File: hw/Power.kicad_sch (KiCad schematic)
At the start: 1 part

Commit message: setup components information
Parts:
- BT?: footprint (none) -> Battery:BatteryHolder_Keystone_2460_1xAA
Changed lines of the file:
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@@
       (effects (font (size 1.27 1.27)) (justify left))
     )
-    (property "Footprint" "" (at 142.24 35.306 90)
+    (property "Footprint" "Battery:BatteryHolder_Keystone_2460_1xAA" (at 142.24 35.306 90)
       (effects (font (size 1.27 1.27)) hide)
     )

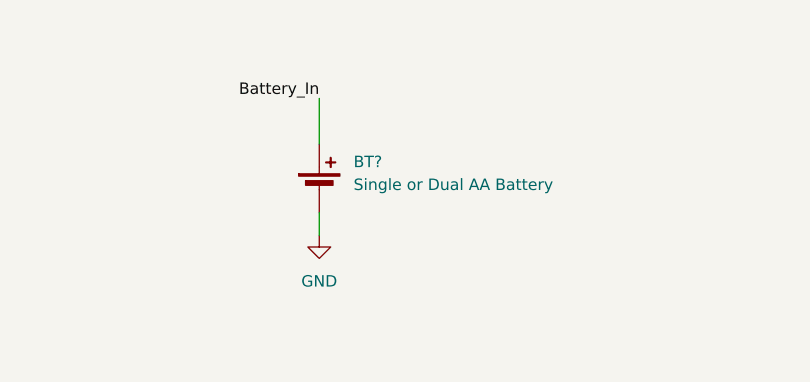
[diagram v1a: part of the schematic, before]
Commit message: added switches
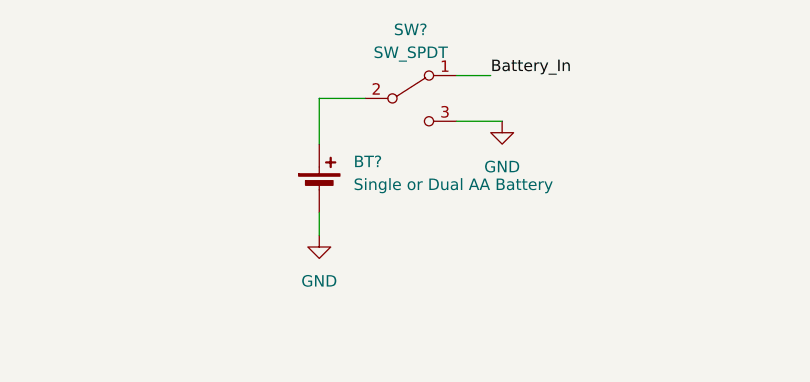
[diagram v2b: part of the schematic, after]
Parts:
- added SW?: SW_SPDT, IotPi_Switch:MS-22D28-G020, symbol Switch:SW_SPDT
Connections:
- net Battery_In: now also SW?.1 (A); no longer BT?.1 (+)
- net GND: now also SW?.3 (C)
- new net: BT?.1 (+), SW?.2 (B)
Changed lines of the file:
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@@
+    (stroke (width 0) (type default))
+  )
+  (wire (pts (xy 157.48 24.13) (xy 161.29 24.13))
+    (stroke (width 0) (type default))
+  )
+  (wire (pts (xy 142.24 26.67) (xy 147.32 26.67))
     (stroke (width 0) (type default))
   )
@@
   )
   (wire (pts (xy 142.24 39.37) (xy 142.24 41.91))
+    (stroke (width 0) (type default))
+  )
+  (wire (pts (xy 157.48 29.21) (xy 162.56 29.21))
     (stroke (width 0) (type default))
   )
@@
     (effects (font (size 1.27 1.27)) (justify right bottom))
   )
-  (label "Battery_In" (at 142.24 26.67 180) (fields_autoplaced)
-    (effects (font (size 1.27 1.27)) (justify right bottom))
+  (label "Battery_In" (at 161.29 24.13 0) (fields_autoplaced)
+    (effects (font (size 1.27 1.27)) (justify left bottom))
   )
   (label "VOUT_3V3" (at 78.74 76.2 180) (fields_autoplaced)
@@
   (hierarchical_label "VBUS" (shape input) (at 43.18 30.48 180) (fields_autoplaced)
     (effects (font (size 1.27 1.27)) (justify right))
+  )
+  (symbol (lib_id "power:GND") (at 162.56 29.21 0) (unit 1)
+    (in_bom yes) (on_board yes) (dnp no) (fields_autoplaced)
+    (property "Reference" "#PWR?" (at 162.56 35.56 0)
+      (effects (font (size 1.27 1.27)) hide)
+    )
+    (property "Value" "GND" (at 162.56 34.29 0)
+      (effects (font (size 1.27 1.27)))
+    )
+    (property "Footprint" "" (at 162.56 29.21 0)
+      (effects (font (size 1.27 1.27)) hide)
+    )
+    (property "Datasheet" "" (at 162.56 29.21 0)
+      (effects (font (size 1.27 1.27)) hide)
+    )
+    (pin "1")
+    (instances
+      (project "KiConSZ2023"
+        (path "/8659c260-f029-4e72-8b9a-85fff45eea40/f453823a-a381-482a-9343-94fafcdcaf18"
+          (reference "#PWR?") (unit 1)
+        )
+      )
+    )
   )
   (symbol (lib_id "Device:Battery_Cell") (at 142.24 36.83 0) (unit 1)
@@
   (symbol (lib_id "power:GND") (at 142.24 41.91 0) (unit 1)
     (in_bom yes) (on_board yes) (dnp no) (fields_autoplaced)
-    (property "Reference" "#PWR05901" (at 142.24 48.26 0)
+    (property "Reference" "#PWR?" (at 142.24 48.26 0)
       (effects (font (size 1.27 1.27)) hide)
     )
@@
       (project "KiConSZ2023"
         (path "/8659c260-f029-4e72-8b9a-85fff45eea40/f453823a-a381-482a-9343-94fafcdcaf18"
-          (reference "#PWR05901") (unit 1)
+          (reference "#PWR?") (unit 1)
         )
       )
+    )
+  )
+  (symbol (lib_id "Switch:SW_SPDT") (at 152.4 26.67 0) (unit 1)
+    (in_bom yes) (on_board yes) (dnp no) (fields_autoplaced)
+    (property "Reference" "SW?" (at 152.4 19.05 0)
+      (effects (font (size 1.27 1.27)))
+    )
+    (property "Value" "SW_SPDT" (at 152.4 21.59 0)
+      (effects (font (size 1.27 1.27)))
+    )
+    (property "Footprint" "IotPi_Switch:MS-22D28-G020" (at 152.4 26.67 0)
+      (effects (font (size 1.27 1.27)) hide)
+    )
+    (property "Datasheet" "~" (at 152.4 26.67 0)
+      (effects (font (size 1.27 1.27)) hide)
+    )
+    (pin "1")
+    (pin "2")
+    (pin "3")
+    (instances
+      (project "KiConSZ2023"
+        (path "/8659c260-f029-4e72-8b9a-85fff45eea40/f453823a-a381-482a-9343-94fafcdcaf18"
+          (reference "SW?") (unit 1)
+        )
+      )

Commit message: annotations
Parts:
- gave numbers to parts that had none: 2
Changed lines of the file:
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@@
   (symbol (lib_id "power:GND") (at 162.56 29.21 0) (unit 1)
     (in_bom yes) (on_board yes) (dnp no) (fields_autoplaced)
-    (property "Reference" "#PWR?" (at 162.56 35.56 0)
+    (property "Reference" "#PWR010" (at 162.56 35.56 0)
       (effects (font (size 1.27 1.27)) hide)
     )
@@
       (project "KiConSZ2023"
         (path "/8659c260-f029-4e72-8b9a-85fff45eea40/f453823a-a381-482a-9343-94fafcdcaf18"
-          (reference "#PWR?") (unit 1)
+          (reference "#PWR010") (unit 1)
         )
       )
@@
   (symbol (lib_id "Device:Battery_Cell") (at 142.24 36.83 0) (unit 1)
     (in_bom yes) (on_board yes) (dnp no) (fields_autoplaced)
-    (property "Reference" "BT?" (at 146.05 33.7185 0)
+    (property "Reference" "BT2" (at 146.05 33.7185 0)
       (effects (font (size 1.27 1.27)) (justify left))
     )
@@
       (project "KiConSZ2023"
         (path "/8659c260-f029-4e72-8b9a-85fff45eea40/f453823a-a381-482a-9343-94fafcdcaf18"
-          (reference "BT?") (unit 1)
+          (reference "BT2") (unit 1)
         )
       )
@@
   (symbol (lib_id "power:GND") (at 142.24 41.91 0) (unit 1)
     (in_bom yes) (on_board yes) (dnp no) (fields_autoplaced)
-    (property "Reference" "#PWR?" (at 142.24 48.26 0)
+    (property "Reference" "#PWR09" (at 142.24 48.26 0)
       (effects (font (size 1.27 1.27)) hide)
     )
@@
       (project "KiConSZ2023"
         (path "/8659c260-f029-4e72-8b9a-85fff45eea40/f453823a-a381-482a-9343-94fafcdcaf18"
-          (reference "#PWR?") (unit 1)
+          (reference "#PWR09") (unit 1)
         )
       )
@@
   (symbol (lib_id "Switch:SW_SPDT") (at 152.4 26.67 0) (unit 1)
     (in_bom yes) (on_board yes) (dnp no) (fields_autoplaced)
-    (property "Reference" "SW?" (at 152.4 19.05 0)
+    (property "Reference" "SW4" (at 152.4 19.05 0)
       (effects (font (size 1.27 1.27)))
     )
@@
       (project "KiConSZ2023"
         (path "/8659c260-f029-4e72-8b9a-85fff45eea40/f453823a-a381-482a-9343-94fafcdcaf18"
-          (reference "SW?") (unit 1)
+          (reference "SW4") (unit 1)
         )
       )

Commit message: updated LCSC of switches
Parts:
- SW4: LCSC (none) -> C963205; Vendor (none) -> G-Switch(品赞); Vendor Model (none) -> MS-22D28-G020
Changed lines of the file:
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@@
+      (effects (font (size 1.27 1.27)) hide)
+    )
+    (property "Description" "额定电流(DC): 1A 额定电压(DC): 6V 电路结构: 双刀双掷 安装方式: 立贴 机械寿命: 10000次 开关颜色: 黑色 滑钮" (at 152.4 26.67 0)
+      (effects (font (size 1.27 1.27)) hide)
+    )
+    (property "LCSC" "C963205" (at 152.4 26.67 0)
+      (effects (font (size 1.27 1.27)) hide)
+    )
+    (property "Vendor" "G-Switch(品赞)" (at 152.4 26.67 0)
+      (effects (font (size 1.27 1.27)) hide)
+    )
+    (property "Vendor Model" "MS-22D28-G020" (at 152.4 26.67 0)
       (effects (font (size 1.27 1.27)) hide)
     )

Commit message: updated netclasses
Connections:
- net Battery_Holder_In: now reaches BT2.1 (+), SW4.2 (B)
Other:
- moved on the sheet: BT2, SW4
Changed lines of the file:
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@@
 (kicad_sch (version 20230121) (generator eeschema)
   (paper "A4")
-  (wire (pts (xy 142.24 31.75) (xy 142.24 26.67))
+  (wire (pts (xy 143.51 35.56) (xy 143.51 40.64))
     (stroke (width 0) (type default))
   )
@@
     (stroke (width 0) (type default))
   )
-  (wire (pts (xy 157.48 24.13) (xy 161.29 24.13))
+  (wire (pts (xy 158.75 33.02) (xy 162.56 33.02))
     (stroke (width 0) (type default))
   )
-  (wire (pts (xy 142.24 26.67) (xy 147.32 26.67))
+  (wire (pts (xy 143.51 35.56) (xy 148.59 35.56))
     (stroke (width 0) (type default))
   )
@@
     (stroke (width 0) (type default))
   )
-  (wire (pts (xy 142.24 39.37) (xy 142.24 41.91))
+  (wire (pts (xy 143.51 48.26) (xy 143.51 50.8))
     (stroke (width 0) (type default))
   )
-  (wire (pts (xy 157.48 29.21) (xy 162.56 29.21))
+  (wire (pts (xy 158.75 38.1) (xy 163.83 38.1))
     (stroke (width 0) (type default))
   )
@@
     (effects (font (size 1.27 1.27)) (justify right bottom))
   )
-  (label "Battery_In" (at 161.29 24.13 0) (fields_autoplaced)
+  (label "Battery_In" (at 162.56 33.02 0) (fields_autoplaced)
+    (effects (font (size 1.27 1.27)) (justify left bottom))
+  )
+  (label "Battery_Holder_In" (at 143.51 35.56 90) (fields_autoplaced)
     (effects (font (size 1.27 1.27)) (justify left bottom))
   )
@@
     (effects (font (size 1.27 1.27)) (justify right))
   )
-  (symbol (lib_id "power:GND") (at 162.56 29.21 0) (unit 1)
+  (netclass_flag "" (length 2.54) (shape round) (at 143.51 40.64 90) (fields_autoplaced)
+    (effects (font (size 1.27 1.27)) (justify left bottom))
+    (property "Netclass" "PWR" (at 140.97 39.9415 90)
+      (effects (font (size 1.27 1.27) italic) (justify left))
+    )
+  )
+  (symbol (lib_id "power:GND") (at 163.83 38.1 0) (unit 1)
     (in_bom yes) (on_board yes) (dnp no) (fields_autoplaced)
-    (property "Reference" "#PWR010" (at 162.56 35.56 0)
+    (property "Reference" "#PWR010" (at 163.83 44.45 0)
       (effects (font (size 1.27 1.27)) hide)
     )
-    (property "Value" "GND" (at 162.56 34.29 0)
+    (property "Value" "GND" (at 163.83 43.18 0)
       (effects (font (size 1.27 1.27)))
     )
-    (property "Footprint" "" (at 162.56 29.21 0)
+    (property "Footprint" "" (at 163.83 38.1 0)
       (effects (font (size 1.27 1.27)) hide)
     )
-    (property "Datasheet" "" (at 162.56 29.21 0)
+    (property "Datasheet" "" (at 163.83 38.1 0)
       (effects (font (size 1.27 1.27)) hide)
     )
@@
     )
   )
-  (symbol (lib_id "Device:Battery_Cell") (at 142.24 36.83 0) (unit 1)
+  (symbol (lib_id "Device:Battery_Cell") (at 143.51 45.72 0) (unit 1)
     (in_bom yes) (on_board yes) (dnp no) (fields_autoplaced)
-    (property "Reference" "BT2" (at 146.05 33.7185 0)
+    (property "Reference" "BT2" (at 147.32 42.6085 0)
       (effects (font (size 1.27 1.27)) (justify left))
     )
-    (property "Value" "Single or Dual AA Battery" (at 146.05 36.2585 0)
+    (property "Value" "Single or Dual AA Battery" (at 147.32 45.1485 0)
       (effects (font (size 1.27 1.27)) (justify left))
     )
-    (property "Footprint" "Battery:BatteryHolder_Keystone_2460_1xAA" (at 142.24 35.306 90)
+    (property "Footprint" "Battery:BatteryHolder_Keystone_2460_1xAA" (at 143.51 44.196 90)
       (effects (font (size 1.27 1.27)) hide)
     )
-    (property "Datasheet" "~" (at 142.24 35.306 90)
+    (property "Datasheet" "~" (at 143.51 44.196 90)
       (effects (font (size 1.27 1.27)) hide)
     )
@@
     )
   )
-  (symbol (lib_id "power:GND") (at 142.24 41.91 0) (unit 1)
+  (symbol (lib_id "power:GND") (at 143.51 50.8 0) (unit 1)
     (in_bom yes) (on_board yes) (dnp no) (fields_autoplaced)
-    (property "Reference" "#PWR09" (at 142.24 48.26 0)
+    (property "Reference" "#PWR09" (at 143.51 57.15 0)
       (effects (font (size 1.27 1.27)) hide)
     )
-    (property "Value" "GND" (at 142.24 46.99 0)
+    (property "Value" "GND" (at 143.51 55.88 0)
       (effects (font (size 1.27 1.27)))
     )
-    (property "Footprint" "" (at 142.24 41.91 0)
+    (property "Footprint" "" (at 143.51 50.8 0)
       (effects (font (size 1.27 1.27)) hide)
     )
-    (property "Datasheet" "" (at 142.24 41.91 0)
+    (property "Datasheet" "" (at 143.51 50.8 0)
       (effects (font (size 1.27 1.27)) hide)
     )
@@
     )
   )
-  (symbol (lib_id "Switch:SW_SPDT") (at 152.4 26.67 0) (unit 1)
+  (symbol (lib_id "Switch:SW_SPDT") (at 153.67 35.56 0) (unit 1)
     (in_bom yes) (on_board yes) (dnp no) (fields_autoplaced)
-    (property "Reference" "SW4" (at 152.4 19.05 0)
+    (property "Reference" "SW4" (at 153.67 27.94 0)
       (effects (font (size 1.27 1.27)))
     )
-    (property "Value" "SW_SPDT" (at 152.4 21.59 0)
+    (property "Value" "SW_SPDT" (at 153.67 30.48 0)
       (effects (font (size 1.27 1.27)))
     )
-    (property "Footprint" "IotPi_Switch:MS-22D28-G020" (at 152.4 26.67 0)
+    (property "Footprint" "IotPi_Switch:MS-22D28-G020" (at 153.67 35.56 0)
       (effects (font (size 1.27 1.27)) hide)
     )
-    (property "Datasheet" "~" (at 152.4 26.67 0)
+    (property "Datasheet" "~" (at 153.67 35.56 0)
       (effects (font (size 1.27 1.27)) hide)
     )
-    (property "Description" "额定电流(DC): 1A 额定电压(DC): 6V 电路结构: 双刀双掷 安装方式: 立贴 机械寿命: 10000次 开关颜色: 黑色 滑钮" (at 152.4 26.67 0)
+    (property "Description" "额定电流(DC): 1A 额定电压(DC): 6V 电路结构: 双刀双掷 安装方式: 立贴 机械寿命: 10000次 开关颜色: 黑色 滑钮" (at 153.67 35.56 0)
       (effects (font (size 1.27 1.27)) hide)
     )
-    (property "LCSC" "C963205" (at 152.4 26.67 0)
+    (property "LCSC" "C963205" (at 153.67 35.56 0)
       (effects (font (size 1.27 1.27)) hide)
     )
-    (property "Vendor" "G-Switch(品赞)" (at 152.4 26.67 0)
+    (property "Vendor" "G-Switch(品赞)" (at 153.67 35.56 0)
       (effects (font (size 1.27 1.27)) hide)
     )
-    (property "Vendor Model" "MS-22D28-G020" (at 152.4 26.67 0)
+    (property "Vendor Model" "MS-22D28-G020" (at 153.67 35.56 0)
       (effects (font (size 1.27 1.27)) hide)
     )

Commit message: updated sheets information
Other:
- company: (none) -> Qingdao IotPi Information Technology Ltd.,
- title: (none) -> KiCad 2023 Shen Zhen Badge
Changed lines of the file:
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@@
 (kicad_sch (version 20230121) (generator eeschema)
   (paper "A4")
+  (title_block
+    (title "KiCad 2023 Shen Zhen Badge")
+    (date "2023-09-04")
+    (rev "1")
+    (company "Qingdao IotPi Information Technology Ltd.,")
+    (comment 1 "Designed by Yang Hongbo")
+  )
   (wire (pts (xy 143.51 35.56) (xy 143.51 40.64))
     (stroke (width 0) (type default))
